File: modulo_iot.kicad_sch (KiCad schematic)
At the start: 4 parts

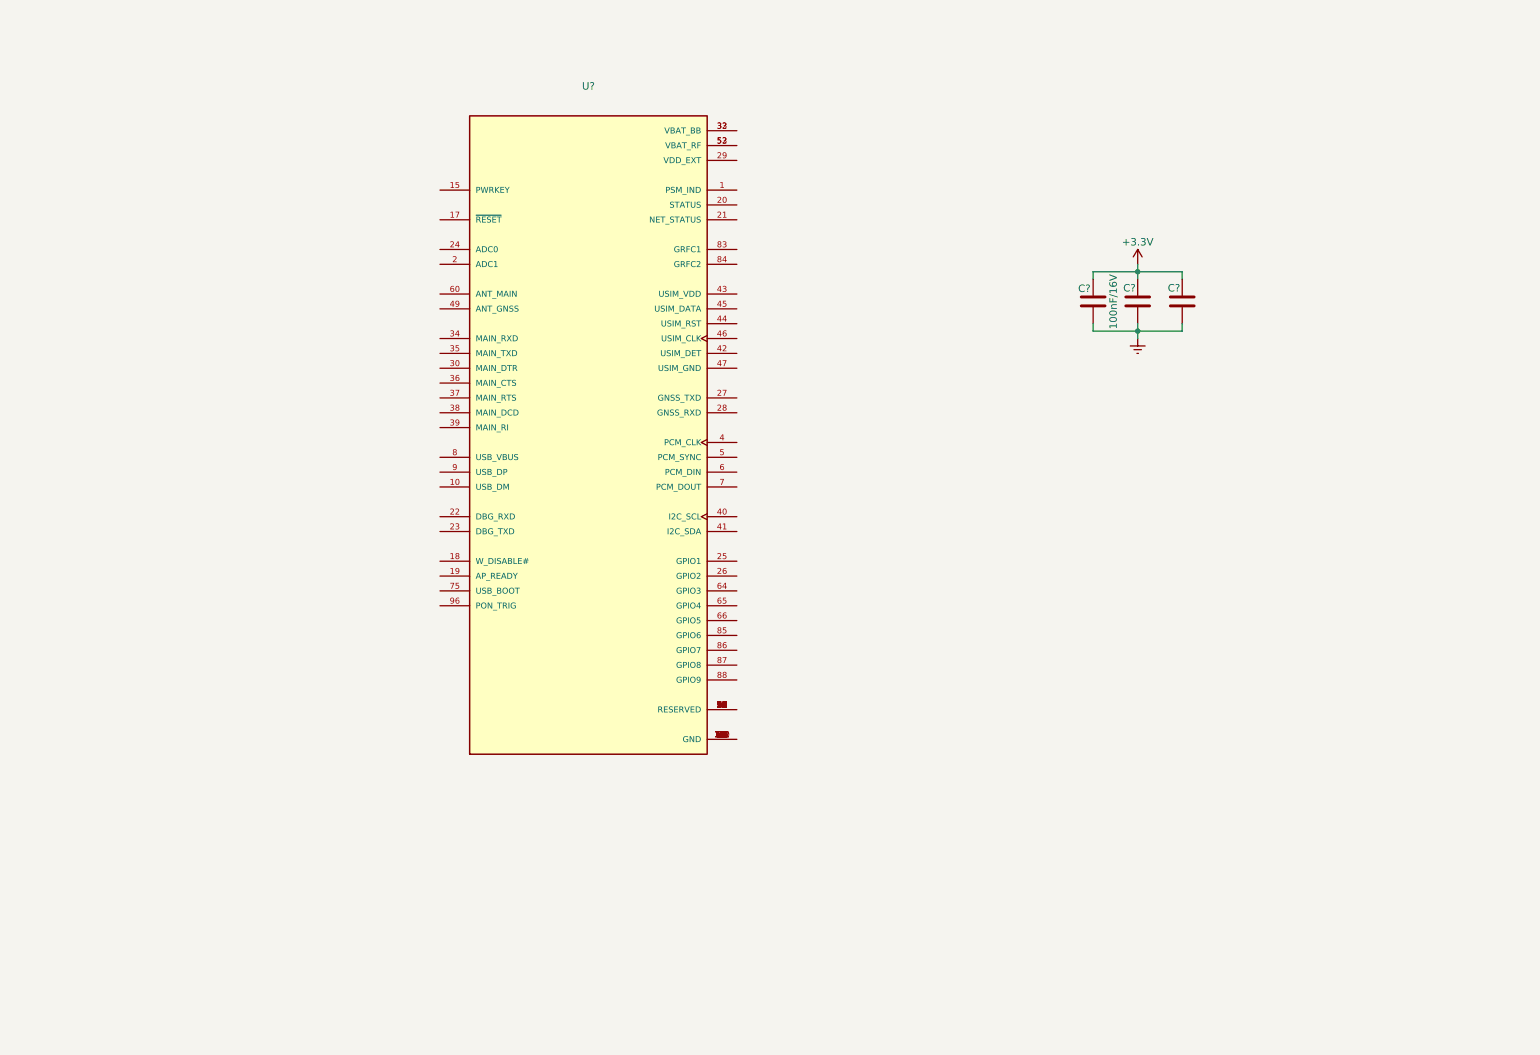
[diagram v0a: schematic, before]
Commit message: Adicionado o circuito de alimentação e reset do BG95
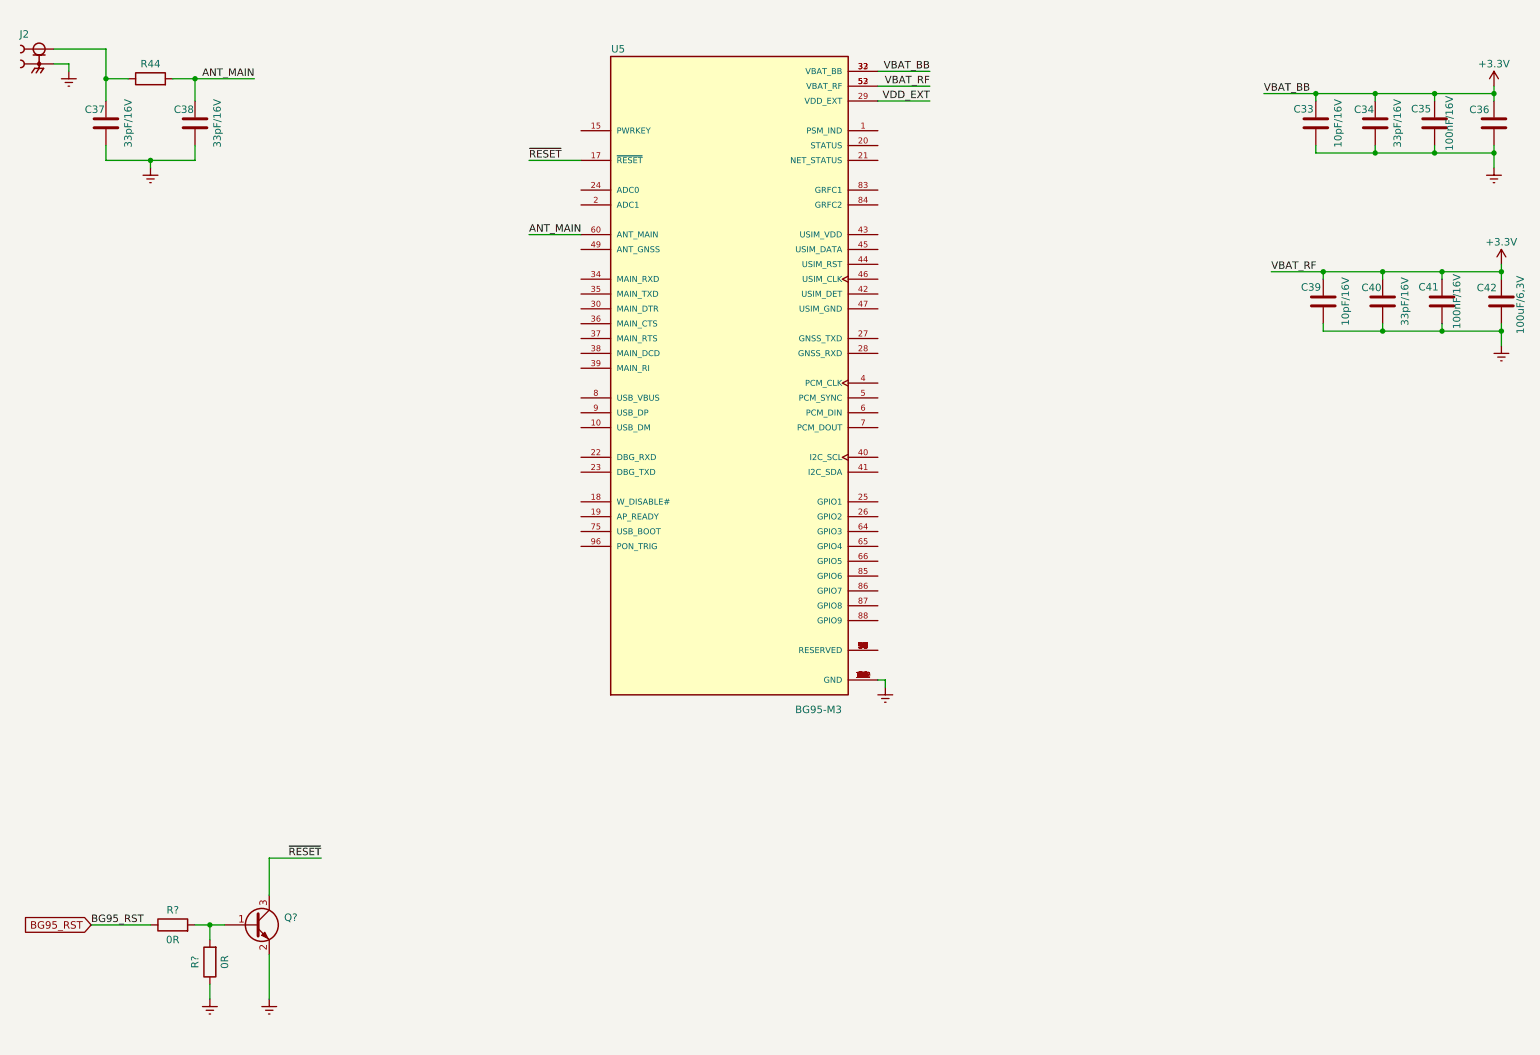
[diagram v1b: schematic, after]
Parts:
- added C36: (no value), symbol Device:C
- added C37, C38, C40: 33pF/16V, Capacitor_SMD:C_0402_1005Metric_Pad0.74x0.62mm_HandSolder, symbol Device:C
- added C39: 10pF/16V, Capacitor_SMD:C_0402_1005Metric_Pad0.74x0.62mm_HandSolder, symbol Device:C
- added C41: 100nF/16V, Capacitor_SMD:C_0402_1005Metric_Pad0.74x0.62mm_HandSolder, symbol Device:C
- added C42: 100uF/6,3V, Capacitor_SMD:C_1206_3216Metric_Pad1.33x1.80mm_HandSolder, symbol Device:C
- added J2: (no value), symbol Alexandre_Library:SMA_CONNECTOR
- added Q?: (no value), symbol Transistor_BJT:BC817
- added R44: (no value), symbol Device:R
- added R? (x2): 0R, Resistor_SMD:R_0402_1005Metric_Pad0.72x0.64mm_HandSolder, symbol Device:R
- C33: renamed from C?; value (none) -> 10pF/16V; footprint (none) -> Capacitor_SMD:C_0402_1005Metric_Pad0.74x0.62mm_HandSolder
- C34: renamed from C?; value (none) -> 33pF/16V; footprint (none) -> Capacitor_SMD:C_0402_1005Metric_Pad0.74x0.62mm_HandSolder
- U5: renamed from U?; value (none) -> BG95-M3; footprint (none) -> BG95:XCVR_BG95
- gave numbers to parts that had none: 1
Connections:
- net +3V3: now also U5.32 (VBAT_BB), U5.33 (VBAT_BB), U5.52 (VBAT_RF), U5.53 (VBAT_RF), C36.1, C39.2, C40.2, C41.2, C42.1
- net GNDREF: now also U5.100 (GND), U5.101 (GND), U5.102 (GND), U5.3 (GND), U5.31 (GND), U5.48 (GND), U5.50 (GND), U5.54 (GND), U5.55 (GND), U5.58 (GND), U5.59 (GND), U5.61 (GND), U5.62 (GND), U5.67 (GND), U5.68 (GND), U5.69 (GND), U5.70 (GND), U5.71 (GND), U5.72 (GND), U5.73 (GND), U5.74 (GND), U5.79 (GND), U5.80 (GND), U5.81 (GND), U5.82 (GND), U5.89 (GND), U5.90 (GND), U5.91 (GND), C36.2, C37.1, C38.1, C39.1, C40.1, C41.1, C42.2, J2.G1, J2.G2, J2.G3, J2.G4, Q?.2 (E), R?.1
- net ~{RESET}: now reaches U5.17 (~{RESET})
- net ~{RESET}: now also Q?.3 (C)
- net VDD_EXT: now reaches U5.29 (VDD_EXT)
- net ANT_MAIN: now reaches U5.60 (ANT_MAIN)
- net ANT_MAIN: now also C38.2, R44.2
- new net: C37.2, J2.1, R44.1
- new net: Q?.1 (B), R?.2, R?.2
- new net BG95_RST: R?.1
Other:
- moved on the sheet: C33, C34, C35, U5

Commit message: Circuito de Reset e Serial TxD do módulo BG95
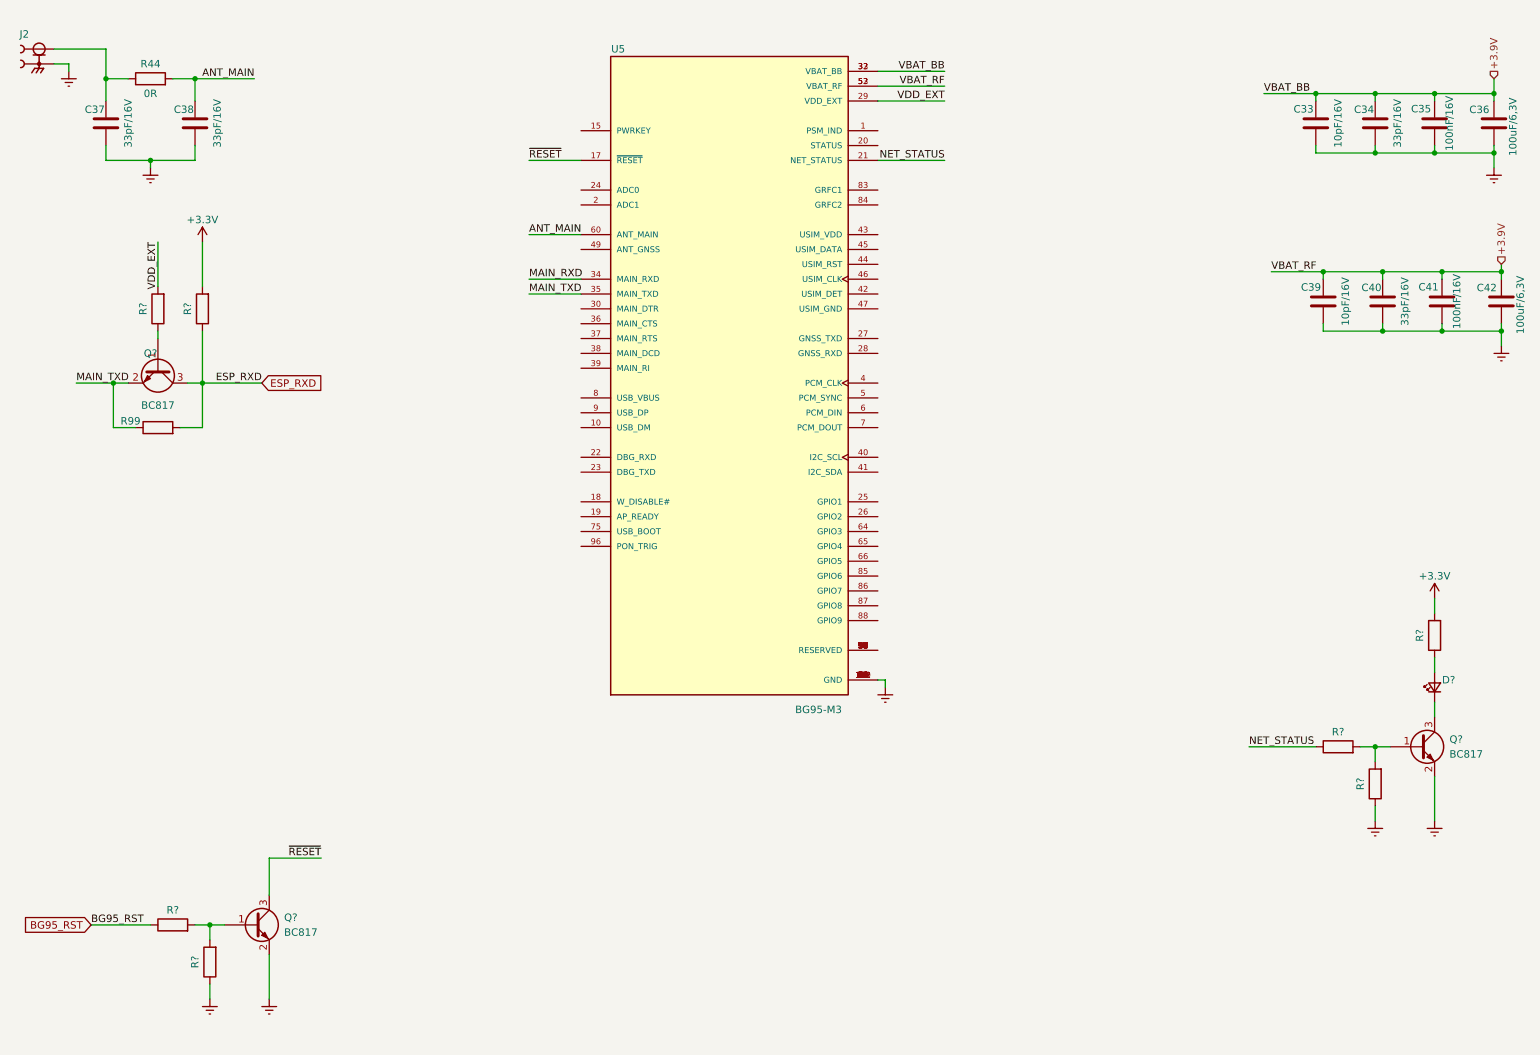
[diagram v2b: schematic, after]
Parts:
- added D?: (no value), symbol Device:LED_Small
- added Q? (x2): BC817, Package_TO_SOT_SMD:SOT-23, symbol Transistor_BJT:BC817
- added R99, R? (x5): (no value), symbol Device:R
- C36: value (none) -> 100uF/6,3V; footprint (none) -> Capacitor_SMD:C_1206_3216Metric_Pad1.33x1.80mm_HandSolder
- J2: value (none) -> SMA_CONNECTOR; footprint (none) -> Alexandre_Library:LPRS_SMA_CONNECTOR
- Q?: value (none) -> BC817; footprint (none) -> Package_TO_SOT_SMD:SOT-23
- R44: value (none) -> 0R; footprint (none) -> Resistor_SMD:R_0402_1005Metric_Pad0.72x0.64mm_HandSolder
- R? (x2): value 0R -> (none); footprint Resistor_SMD:R_0402_1005Metric_Pad0.72x0.64mm_HandSolder -> (none)
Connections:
- net +3V3: now also R?.2, R?.2; no longer C33.2, C34.2, C35.2, C36.1, C39.2, C40.2, C41.2, C42.1, U5.32 (VBAT_BB), U5.33 (VBAT_BB), U5.52 (VBAT_RF), U5.53 (VBAT_RF)
- net GNDREF: now also Q?.2 (E), R?.1
- net VDD_EXT: now also R?.2
- net NET_STATUS: now reaches U5.21 (NET_STATUS)
- net NET_STATUS: now also R?.1
- net MAIN_RXD: now reaches U5.34 (MAIN_RXD)
- net MAIN_TXD: now reaches U5.35 (MAIN_TXD)
- net MAIN_TXD: now also Q?.2 (E), R99.1
- new net: Q?.1 (B), R?.2, R?.2
- new net: D?.2 (A), R?.1
- new net: Q?.1 (B), R?.1
- new net: D?.1 (K), Q?.3 (C)
- new net +3.9V: C33.2, C34.2, C35.2, C36.1, C39.2, C40.2, C41.2, C42.1, U5.32 (VBAT_BB), U5.33 (VBAT_BB), U5.52 (VBAT_RF), U5.53 (VBAT_RF)
- new net ESP_RXD: Q?.3 (C), R99.2, R?.1

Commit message: Adicionado os circuitos de RxD, NEt Status, Status do módulo BG95
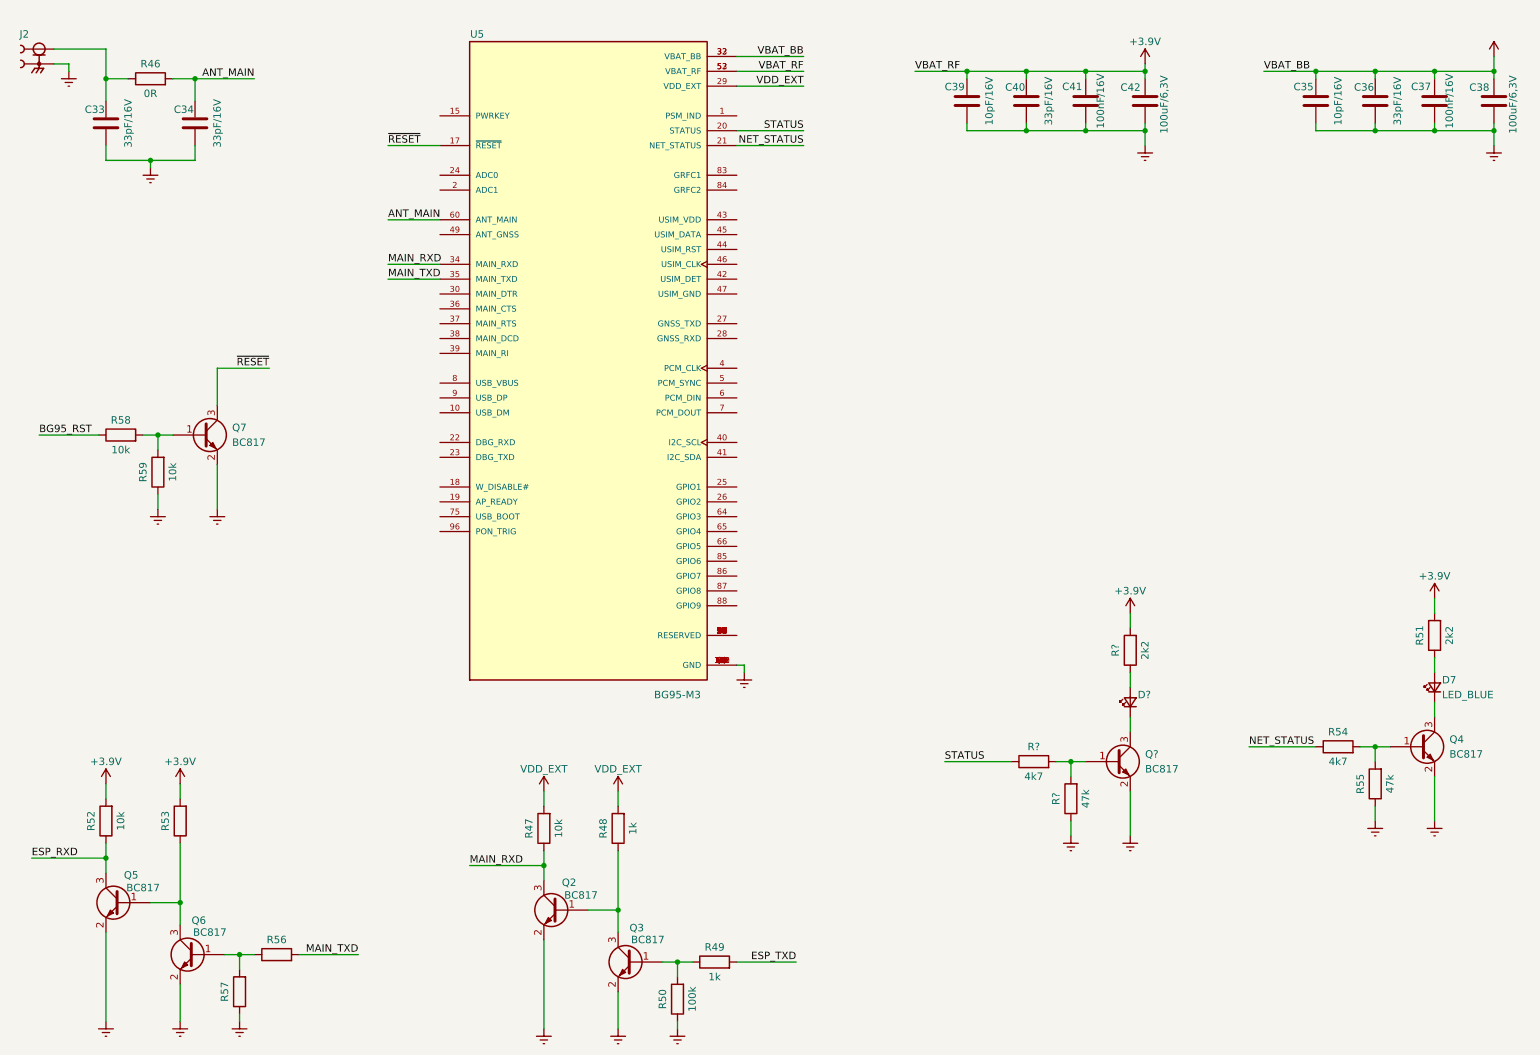
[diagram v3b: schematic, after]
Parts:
- removed Q?: BC817, Package_TO_SOT_SMD:SOT-23, symbol Transistor_BJT:BC817
- removed R99, R? (x2): (no value), symbol Device:R
- added D?: (no value), symbol Device:LED_Small
- added Q2, Q3, Q5, Q6, Q?: BC817, Package_TO_SOT_SMD:SOT-23, symbol Transistor_BJT:BC817
- added R47, R52: 10k, Resistor_SMD:R_0402_1005Metric_Pad0.72x0.64mm_HandSolder, symbol Device:R
- added R48, R49: 1k, Resistor_SMD:R_0402_1005Metric_Pad0.72x0.64mm_HandSolder, symbol Device:R
- added R50: 100k, Resistor_SMD:R_0402_1005Metric_Pad0.72x0.64mm_HandSolder, symbol Device:R
- added R53: (no value), symbol Device:R
- added R56, R57: (no value), Resistor_SMD:R_0402_1005Metric_Pad0.72x0.64mm_HandSolder, symbol Device:R
- added R?: 2k2, Resistor_SMD:R_0402_1005Metric_Pad0.72x0.64mm_HandSolder, symbol Device:R
- added R?: 4k7, Resistor_SMD:R_0402_1005Metric_Pad0.72x0.64mm_HandSolder, symbol Device:R
- added R?: 47k, Resistor_SMD:R_0402_1005Metric_Pad0.72x0.64mm_HandSolder, symbol Device:R
- D7: renamed from D?; value (none) -> LED_BLUE; footprint (none) -> LED_SMD:LED_0603_1608Metric_Pad1.05x0.95mm_HandSolder
- R51: renamed from R?; value (none) -> 2k2; footprint (none) -> Resistor_SMD:R_0402_1005Metric_Pad0.72x0.64mm_HandSolder
- R54: renamed from R?; value (none) -> 4k7; footprint (none) -> Resistor_SMD:R_0402_1005Metric_Pad0.72x0.64mm_HandSolder
- R55: renamed from R?; value (none) -> 47k; footprint (none) -> Resistor_SMD:R_0402_1005Metric_Pad0.72x0.64mm_HandSolder
- R58, R59: renamed from R?; value (none) -> 10k; footprint (none) -> Resistor_SMD:R_0402_1005Metric_Pad0.72x0.64mm_HandSolder
- gave numbers to parts that had none: 2
- renumbered C37 to C33, C38 to C34, C33 to C35, C34 to C36, C35 to C37, C36 to C38, R44 to R46
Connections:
- net ESP_RXD: now also Q5.3 (C), R52.1
- net GNDREF: now also Q2.2 (E), Q3.2 (E), Q5.2 (E), Q6.2 (E), Q?.2 (E), R50.1, R57.1, R?.1
- net MAIN_RXD: now also Q2.3 (C), R47.1
- net MAIN_TXD: now also R56.2
- net STATUS: now reaches U5.20 (STATUS)
- net STATUS: now also R?.1
- net +3.9V renamed VBAT_BB
- net VBAT_BB: no longer C39.2, C40.2, C41.2, C42.1, U5.52 (VBAT_RF), U5.53 (VBAT_RF)
- net +3V3: no longer names the net of R51.2
- new net: Q2.1 (B), Q3.3 (C), R48.1
- new net: D?.2 (A), R?.1
- new net: Q3.1 (B), R49.1, R50.2
- new net: Q5.1 (B), Q6.3 (C), R53.1
- new net: Q6.1 (B), R56.1, R57.2
- new net: Q?.1 (B), R?.2, R?.2
- new net: D?.1 (K), Q?.3 (C)
- new net ESP_TXD: R49.2
- new net VBAT_RF: C39.2, C40.2, C41.2, C42.1, U5.52 (VBAT_RF), U5.53 (VBAT_RF)
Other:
- moved on the sheet: C35, C36, C37, C38, C39, C40, C41, C42, Q7, R58, R59, U5
